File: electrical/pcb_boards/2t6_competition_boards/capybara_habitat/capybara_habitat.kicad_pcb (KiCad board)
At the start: 2 copper layers, 137.3 x 78 mm, 118 parts, among them J1 Barrel_Jack, J10 monitor2_power, J11 aud_sig_out_a, J12 spare_usb_2nd_disp_pwr, J13 2nd_disp_sw, J14 spkrs_sw, J15 Raspberry_Pi_4, J16 Raspberry_Pi_4, J2 leds_power, J3 monitor1_power, J4 charger_buck_in, J5 leds_sw, J6 1st_disp_sw, J7 aud_sig_out_b, J8 vbatt, J9 aud_sig_in, U1 TPS22810DBV, U2 TPS22810DBV, U3 TPS22810DBV, U4 Adafruit_INA219, U5 Adafruit_INA219, U6 PAM8406D, U7 TPS22810DBV, U8 LT8610ABEMSE-5-TRPBF, U9 LTC3114IFE-1_TRPBF

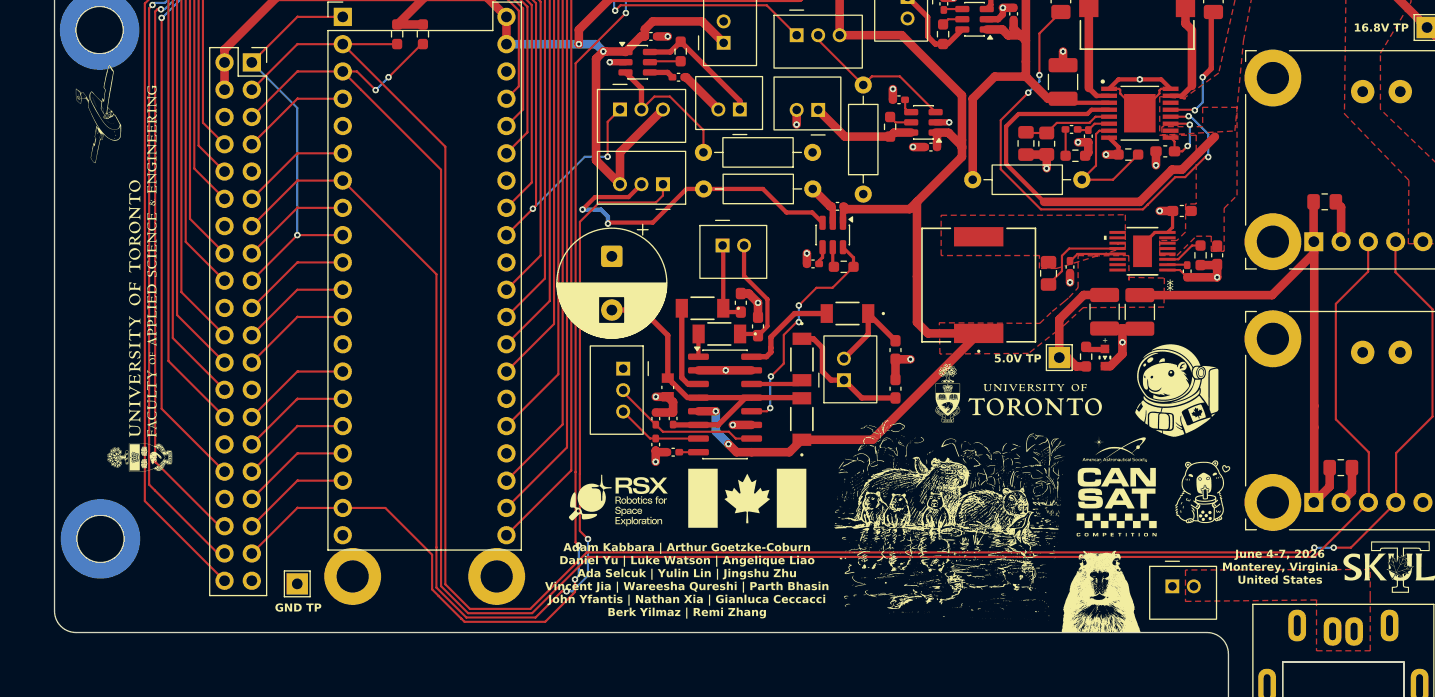
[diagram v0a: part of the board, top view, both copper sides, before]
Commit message: silk screen edits + power jst
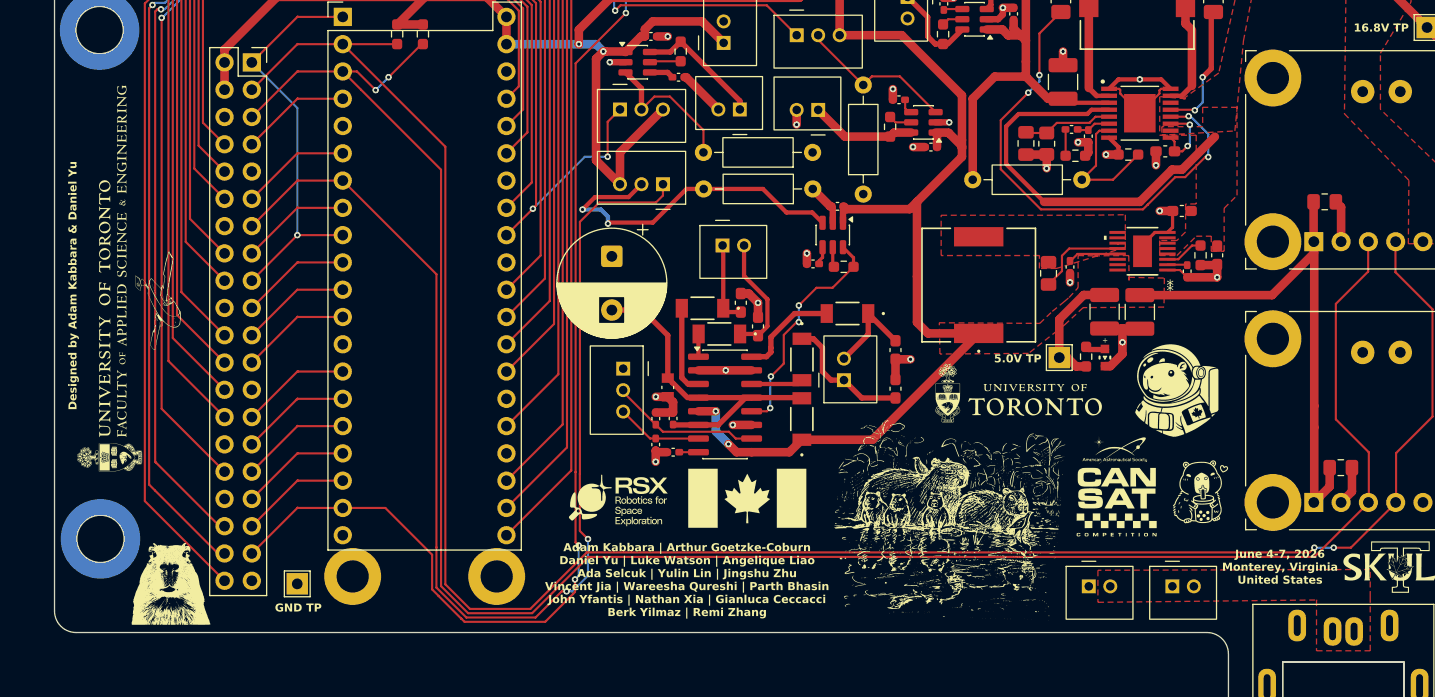
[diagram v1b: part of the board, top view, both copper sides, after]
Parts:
- added J17: charger_buck_in, RSX_CanSat_Custom_KiCad_Footprints:J_Wurth_WR-WTB_62000211622, F.Cu at (207.0, 126.8)
- moved G*** 86.6 mm to (121.4, 125.9)
- moved G*** 18.3 mm to (120.0, 100.2)
- moved G*** 2.80 mm to (115.8, 98.1)
- moved G*** 0.20 mm to (217.4, 118.0)
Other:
- board text added: "Designed by Adam Kabbara & Daniel Yu"

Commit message: Finalizing ground station design
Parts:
- added G***: LOGO, LOGO, F.Cu at (133.4, 75.6)
- moved R10 16.9 mm to (128.2, 73.8)
- moved R11 12.7 mm to (130.0, 73.8)
- moved G*** 2.18 mm to (121.0, 98.2)
- moved G*** 0.82 mm to (217.6, 117.2)
- moved G*** 0.60 mm to (209.6, 116.8)
- moved G*** 0.57 mm to (215.6, 108.2)
- moved G*** 0.51 mm to (116.3, 98.0)
- moved G*** 0.40 mm to (193.8, 121.0)
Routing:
- net 5.0v: track 273.9 -> 269.1 mm
- net Net-(J15-3V3-Pad1): track 38.3 -> 41.8 mm, vias 1 -> 0
- net SCL: track 190.6 -> 188.1 mm
- net SDA: track 190.2 -> 189.2 mm, vias 2 -> 4
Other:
- board text added: "Audio In"
- board text added: "Audio Out L"
- board text added: "Audio Out R"
- board text added: "Charger Buck In"
- board text added: "Col A"
- board text added: "Col B"
- board text added: "Disp1 PWR"
- board text added: "Disp1 SW"
- board text added: "Disp2 PWR"
- board text added: "Disp2 SW"
- board text added: "LED PWR"
- board text added: "LED SW"
- board text added: "Speaker SW"
- board text added: "USB2 PWR"
- board text added: "VBatt"
